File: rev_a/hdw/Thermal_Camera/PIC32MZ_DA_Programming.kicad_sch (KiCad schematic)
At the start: 17 parts

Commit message: added some power supplies
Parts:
- added J?: MRST, symbol Connector_Generic:Conn_02x01
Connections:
- net +3.3V: now also J?.1 (Pin_1)
- net at R?.1, SW?.2: now also J?.2 (Pin_2)
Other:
- moved on the sheet: SW?
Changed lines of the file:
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@@
     (company "Drew Maatman and Michael Laffin")
   )
+  (junction (at 69.85 139.7) (diameter 0) (color 0 0 0 0)
+  )
   (junction (at 106.68 139.7) (diameter 0) (color 0 0 0 0)
+  )
+  (junction (at 86.36 139.7) (diameter 0) (color 0 0 0 0)
   )
   (junction (at 96.52 49.53) (diameter 0) (color 0 0 0 0)
@@
     (stroke (width 0) (type default))
   )
+  (wire (pts (xy 86.36 139.7) (xy 83.82 139.7))
+    (stroke (width 0) (type default))
+  )
   (wire (pts (xy 102.87 71.12) (xy 102.87 54.61))
     (stroke (width 0) (type default))
@@
     (stroke (width 0) (type default))
   )
+  (wire (pts (xy 86.36 139.7) (xy 86.36 147.32))
+    (stroke (width 0) (type default))
+  )
   (wire (pts (xy 90.17 71.12) (xy 90.17 46.99))
     (stroke (width 0) (type default))
@@
     (stroke (width 0) (type default))
   )
+  (wire (pts (xy 72.39 147.32) (xy 69.85 147.32))
+    (stroke (width 0) (type default))
+  )
   (wire (pts (xy 135.255 52.07) (xy 176.53 52.07))
     (stroke (width 0) (type default))
@@
     (stroke (width 0) (type default))
   )
-  (wire (pts (xy 74.93 139.7) (xy 78.74 139.7))
+  (wire (pts (xy 85.09 147.32) (xy 86.36 147.32))
+    (stroke (width 0) (type default))
+  )
+  (wire (pts (xy 69.85 139.7) (xy 73.66 139.7))
     (stroke (width 0) (type default))
   )
@@
     (stroke (width 0) (type default))
   )
+  (wire (pts (xy 69.85 147.32) (xy 69.85 139.7))
+    (stroke (width 0) (type default))
+  )
   (wire (pts (xy 134.62 126.365) (xy 147.955 126.365))
     (stroke (width 0) (type default))
   )
-  (wire (pts (xy 74.93 138.43) (xy 74.93 139.7))
-    (stroke (width 0) (type default))
-  )
-  (wire (pts (xy 91.44 139.7) (xy 88.9 139.7))
+  (wire (pts (xy 69.85 138.43) (xy 69.85 139.7))
+    (stroke (width 0) (type default))
+  )
+  (wire (pts (xy 91.44 139.7) (xy 86.36 139.7))
     (stroke (width 0) (type default))
   )
@@
     )
   )
-  (symbol (lib_id "Switch:SW_Push") (at 83.82 139.7 0) (unit 1)
-    (in_bom yes) (on_board yes) (dnp no)
-    (property "Reference" "SW?" (at 83.82 132.461 0)
-      (effects (font (size 1.27 1.27)))
-    )
-    (property "Value" "MRST" (at 83.82 134.7724 0)
-      (effects (font (size 1.27 1.27)))
-    )
-    (property "Footprint" "Button_Switch_THT:SW_PUSH_6mm" (at 83.82 134.62 0)
-      (effects (font (size 1.27 1.27)) hide)
-    )
-    (property "Datasheet" "" (at 83.82 134.62 0)
+  (symbol (lib_id "Switch:SW_Push") (at 78.74 139.7 0) (unit 1)
+    (in_bom yes) (on_board yes) (dnp no)
+    (property "Reference" "SW?" (at 78.74 132.461 0)
+      (effects (font (size 1.27 1.27)))
+    )
+    (property "Value" "MRST" (at 78.74 134.7724 0)
+      (effects (font (size 1.27 1.27)))
+    )
+    (property "Footprint" "Button_Switch_THT:SW_PUSH_6mm" (at 78.74 134.62 0)
+      (effects (font (size 1.27 1.27)) hide)
+    )
+    (property "Datasheet" "" (at 78.74 134.62 0)
       (effects (font (size 1.27 1.27)) hide)
     )
@@
         (path "/4bd21e0b-5408-4b93-866e-c82ac5b31fa9/c8b41008-ee29-40ae-a4f4-13001b750237"
           (reference "SW?") (unit 1)
+        )
+      )
+    )
+  )
+  (symbol (lib_id "Connector_Generic:Conn_02x01") (at 77.47 147.32 0) (unit 1)
+    (in_bom yes) (on_board yes) (dnp no)
+    (property "Reference" "J?" (at 78.74 144.78 0)
+      (effects (font (size 1.27 1.27)))
+    )
+    (property "Value" "MRST" (at 78.74 149.86 0)
+      (effects (font (size 1.27 1.27)))
+    )
+    (property "Footprint" "" (at 77.47 147.32 0)
+      (effects (font (size 1.27 1.27)) hide)
+    )
+    (property "Datasheet" "~" (at 77.47 147.32 0)
+      (effects (font (size 1.27 1.27)) hide)
+    )
+    (pin "2")
+    (pin "1")
+    (instances
+      (project "Thermal_Camera"
+        (path "/4bd21e0b-5408-4b93-866e-c82ac5b31fa9/c8b41008-ee29-40ae-a4f4-13001b750237"
+          (reference "J?") (unit 1)
         )
       )
@@
     )
   )
-  (symbol (lib_id "power:+3.3V") (at 74.93 138.43 0) (unit 1)
-    (in_bom yes) (on_board yes) (dnp no)
-    (property "Reference" "#PWR?" (at 74.93 142.24 0)
-      (effects (font (size 1.27 1.27)) hide)
-    )
-    (property "Value" "+3.3V" (at 74.93 134.874 0)
-      (effects (font (size 1.27 1.27)))
-    )
-    (property "Footprint" "" (at 74.93 138.43 0)
-      (effects (font (size 1.27 1.27)) hide)
-    )
-    (property "Datasheet" "" (at 74.93 138.43 0)
-      (effects (font (size 1.27 1.27)) hide)
-    )
+  (symbol (lib_id "power:+3.3V") (at 69.85 138.43 0) (unit 1)
+    (in_bom yes) (on_board yes) (dnp no)
+    (property "Reference" "#PWR?" (at 69.85 142.24 0)
+      (effects (font (size 1.27 1.27)) hide)
+    )
+    (property "Value" "+3.3V" (at 69.85 134.874 0)
+      (effects (font (size 1.27 1.27)))
+    )
+    (property "Footprint" "" (at 69.85 138.43 0)
+      (effects (font (size 1.27 1.27)) hide)
+    )
+    (property "Datasheet" "" (at 69.85 138.43 0)
+      (effects (font (size 1.27 1.27)) hide)
+    )

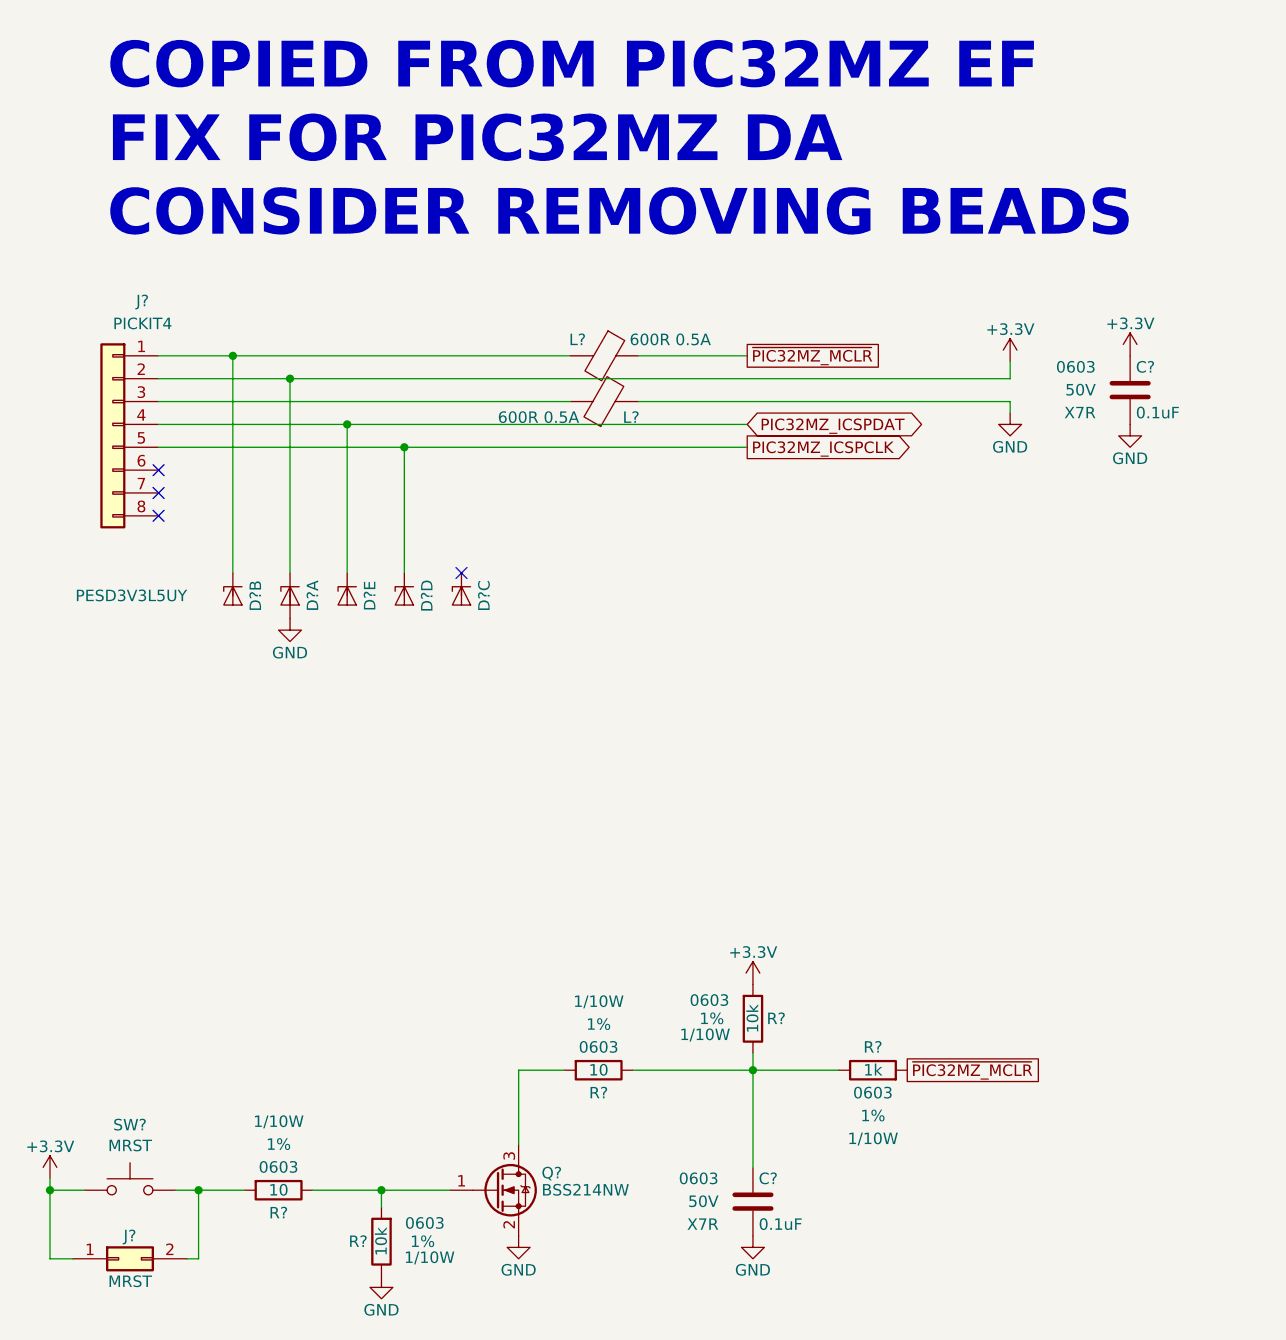
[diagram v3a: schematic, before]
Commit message: changed a lot of circuits from +3.3V to +3.0V VDD
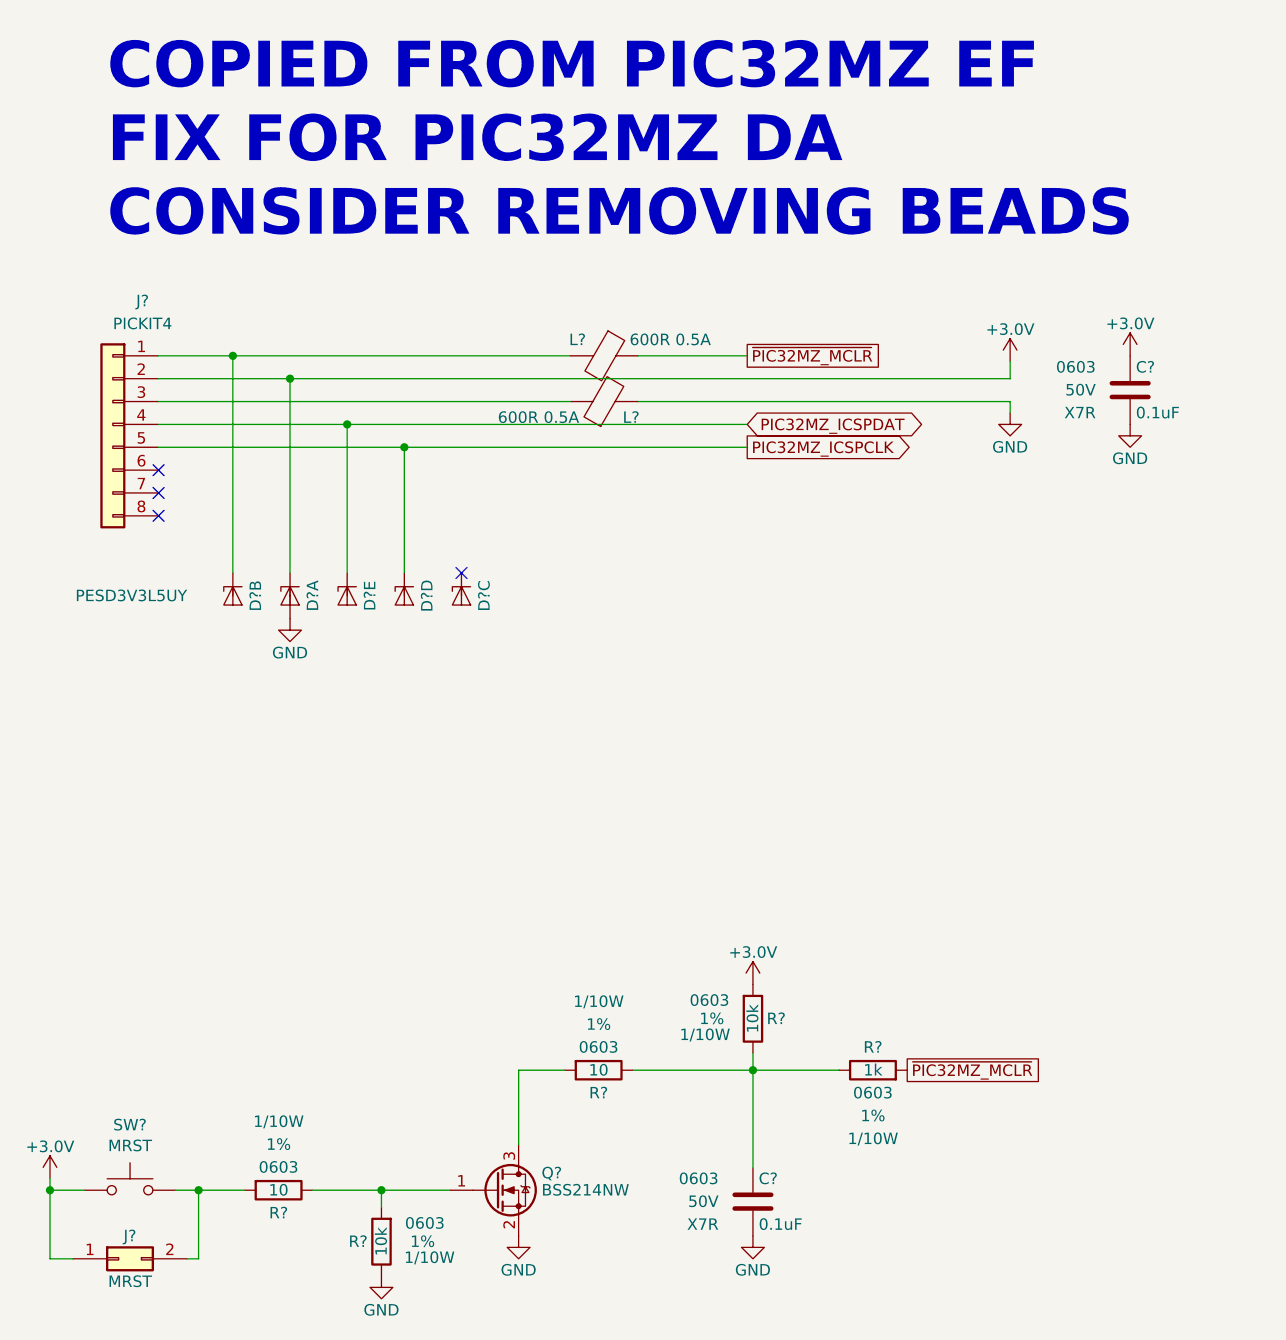
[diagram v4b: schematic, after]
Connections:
- net +3.3V renamed +3.0V
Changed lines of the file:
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@@
+    )
+  )
+  (symbol (lib_id "Custom Library:+3.0V") (at 147.955 116.84 0) (unit 1)
+    (in_bom yes) (on_board yes) (dnp no)
+    (property "Reference" "#PWR01503" (at 147.955 120.65 0)
+      (effects (font (size 1.27 1.27)) hide)
+    )
+    (property "Value" "+3.0V" (at 147.955 113.284 0)
+      (effects (font (size 1.27 1.27)))
+    )
+    (property "Footprint" "" (at 147.955 116.84 0)
+      (effects (font (size 1.27 1.27)) hide)
+    )
+    (property "Datasheet" "" (at 147.955 116.84 0)
+      (effects (font (size 1.27 1.27)) hide)
+    )
+    (pin "1")
+    (instances
+      (project "Thermal_Camera"
+        (path "/4bd21e0b-5408-4b93-866e-c82ac5b31fa9/c8b41008-ee29-40ae-a4f4-13001b750237"
+          (reference "#PWR01503") (unit 1)
+        )
+      )
     )
   )
@@
     )
   )
+  (symbol (lib_id "Custom Library:+3.0V") (at 69.85 138.43 0) (unit 1)
+    (in_bom yes) (on_board yes) (dnp no)
+    (property "Reference" "#PWR01504" (at 69.85 142.24 0)
+      (effects (font (size 1.27 1.27)) hide)
+    )
+    (property "Value" "+3.0V" (at 69.85 134.874 0)
+      (effects (font (size 1.27 1.27)))
+    )
+    (property "Footprint" "" (at 69.85 138.43 0)
+      (effects (font (size 1.27 1.27)) hide)
+    )
+    (property "Datasheet" "" (at 69.85 138.43 0)
+      (effects (font (size 1.27 1.27)) hide)
+    )
+    (pin "1")
+    (instances
+      (project "Thermal_Camera"
+        (path "/4bd21e0b-5408-4b93-866e-c82ac5b31fa9/c8b41008-ee29-40ae-a4f4-13001b750237"
+          (reference "#PWR01504") (unit 1)
+        )
+      )
+    )
+  )
   (symbol (lib_id "Power_Protection:PESD3V3L5UY") (at 90.17 73.66 270) (unit 2)
     (in_bom yes) (on_board yes) (dnp no)
@@
     )
   )
-  (symbol (lib_id "power:+3.3V") (at 147.955 116.84 0) (unit 1)
-    (in_bom yes) (on_board yes) (dnp no)
-    (property "Reference" "#PWR?" (at 147.955 120.65 0)
-      (effects (font (size 1.27 1.27)) hide)
-    )
-    (property "Value" "+3.3V" (at 147.955 113.284 0)
-      (effects (font (size 1.27 1.27)))
-    )
-    (property "Footprint" "" (at 147.955 116.84 0)
-      (effects (font (size 1.27 1.27)) hide)
-    )
-    (property "Datasheet" "" (at 147.955 116.84 0)
-      (effects (font (size 1.27 1.27)) hide)
-    )
-    (pin "1")
-    (instances
-      (project "Analog_Clock"
-        (path "/0dc9b974-a945-4291-bc55-04b8e342b0e5/00000000-0000-0000-0000-00005e939eaf"
-          (reference "#PWR?") (unit 1)
-        )
-      )
-      (project "Nixie_Clock_Core"
-        (path "/16fdce21-b570-4d81-a458-e8839d611806/0953f70f-0c64-48c1-b5cf-d1f41f95ef1f"
-          (reference "#PWR0805") (unit 1)
-        )
-      )
-      (project "Thermal_Camera"
-        (path "/4bd21e0b-5408-4b93-866e-c82ac5b31fa9/c8b41008-ee29-40ae-a4f4-13001b750237"
-          (reference "#PWR0905") (unit 1)
-        )
-      )
-    )
-  )
   (symbol (lib_id "Custom_Library:C_Custom") (at 189.865 50.8 0) (unit 1)
     (in_bom yes) (on_board yes) (dnp no)
@@
         (path "/4bd21e0b-5408-4b93-866e-c82ac5b31fa9/c8b41008-ee29-40ae-a4f4-13001b750237"
           (reference "C?") (unit 1)
+        )
+      )
+    )
+  )
+  (symbol (lib_id "Custom Library:+3.0V") (at 176.53 47.625 0) (unit 1)
+    (in_bom yes) (on_board yes) (dnp no)
+    (property "Reference" "#PWR01502" (at 176.53 51.435 0)
+      (effects (font (size 1.27 1.27)) hide)
+    )
+    (property "Value" "+3.0V" (at 176.53 44.069 0)
+      (effects (font (size 1.27 1.27)))
+    )
+    (property "Footprint" "" (at 176.53 47.625 0)
+      (effects (font (size 1.27 1.27)) hide)
+    )
+    (property "Datasheet" "" (at 176.53 47.625 0)
+      (effects (font (size 1.27 1.27)) hide)
+    )
+    (pin "1")
+    (instances
+      (project "Thermal_Camera"
+        (path "/4bd21e0b-5408-4b93-866e-c82ac5b31fa9/c8b41008-ee29-40ae-a4f4-13001b750237"
+          (reference "#PWR01502") (unit 1)
         )
       )
@@
     )
   )
-  (symbol (lib_id "power:+3.3V") (at 176.53 47.625 0) (unit 1)
-    (in_bom yes) (on_board yes) (dnp no)
-    (property "Reference" "#PWR?" (at 176.53 51.435 0)
-      (effects (font (size 1.27 1.27)) hide)
-    )
-    (property "Value" "+3.3V" (at 176.53 44.069 0)
-      (effects (font (size 1.27 1.27)))
-    )
-    (property "Footprint" "" (at 176.53 47.625 0)
-      (effects (font (size 1.27 1.27)) hide)
-    )
-    (property "Datasheet" "" (at 176.53 47.625 0)
-      (effects (font (size 1.27 1.27)) hide)
-    )
-    (pin "1")
-    (instances
-      (project "Analog_Clock"
-        (path "/0dc9b974-a945-4291-bc55-04b8e342b0e5/00000000-0000-0000-0000-00005e939eaf"
-          (reference "#PWR?") (unit 1)
-        )
-      )
-      (project "Nixie_Clock_Core"
-        (path "/16fdce21-b570-4d81-a458-e8839d611806/0953f70f-0c64-48c1-b5cf-d1f41f95ef1f"
-          (reference "#PWR0807") (unit 1)
-        )
-      )
-      (project "Thermal_Camera"
-        (path "/4bd21e0b-5408-4b93-866e-c82ac5b31fa9/c8b41008-ee29-40ae-a4f4-13001b750237"
-          (reference "#PWR0907") (unit 1)
-        )
-      )
-    )
-  )
   (symbol (lib_id "Power_Protection:PESD3V3L5UY") (at 109.22 73.66 270) (unit 4)
     (in_bom yes) (on_board yes) (dnp no)
@@
     )
   )
+  (symbol (lib_id "Custom Library:+3.0V") (at 189.865 46.99 0) (unit 1)
+    (in_bom yes) (on_board yes) (dnp no)
+    (property "Reference" "#PWR01501" (at 189.865 50.8 0)
+      (effects (font (size 1.27 1.27)) hide)
+    )
+    (property "Value" "+3.0V" (at 189.865 43.434 0)
+      (effects (font (size 1.27 1.27)))
+    )
+    (property "Footprint" "" (at 189.865 46.99 0)
+      (effects (font (size 1.27 1.27)) hide)
+    )
+    (property "Datasheet" "" (at 189.865 46.99 0)
+      (effects (font (size 1.27 1.27)) hide)
+    )
+    (pin "1")
+    (instances
+      (project "Thermal_Camera"
+        (path "/4bd21e0b-5408-4b93-866e-c82ac5b31fa9/c8b41008-ee29-40ae-a4f4-13001b750237"
+          (reference "#PWR01501") (unit 1)
+        )
+      )
+    )
+  )
   (symbol (lib_id "Custom_Library:C_Custom") (at 147.955 140.97 0) (unit 1)
     (in_bom yes) (on_board yes) (dnp no)
@@
     )
   )
-  (symbol (lib_id "power:+3.3V") (at 69.85 138.43 0) (unit 1)
-    (in_bom yes) (on_board yes) (dnp no)
-    (property "Reference" "#PWR?" (at 69.85 142.24 0)
-      (effects (font (size 1.27 1.27)) hide)
-    )
-    (property "Value" "+3.3V" (at 69.85 134.874 0)
-      (effects (font (size 1.27 1.27)))
-    )
-    (property "Footprint" "" (at 69.85 138.43 0)
-      (effects (font (size 1.27 1.27)) hide)
-    )
-    (property "Datasheet" "" (at 69.85 138.43 0)
-      (effects (font (size 1.27 1.27)) hide)
-    )
-    (pin "1")
-    (instances
-      (project "Analog_Clock"
-        (path "/0dc9b974-a945-4291-bc55-04b8e342b0e5/00000000-0000-0000-0000-00005e939eaf"
-          (reference "#PWR?") (unit 1)
-        )
-      )
-      (project "Nixie_Clock_Core"
-        (path "/16fdce21-b570-4d81-a458-e8839d611806/0953f70f-0c64-48c1-b5cf-d1f41f95ef1f"
-          (reference "#PWR0801") (unit 1)
-        )
-      )
-      (project "Thermal_Camera"
-        (path "/4bd21e0b-5408-4b93-866e-c82ac5b31fa9/c8b41008-ee29-40ae-a4f4-13001b750237"
-          (reference "#PWR0901") (unit 1)
-        )
-      )
-    )
-  )
   (symbol (lib_id "Device:Ferrite_Bead") (at 131.445 46.99 270) (unit 1)
     (in_bom yes) (on_board yes) (dnp no)
@@
         )
       )
-    )
-  )
-  (symbol (lib_id "power:+3.3V") (at 189.865 46.99 0) (unit 1)
-    (in_bom yes) (on_board yes) (dnp no)
-    (property "Reference" "#PWR?" (at 189.865 50.8 0)
-      (effects (font (size 1.27 1.27)) hide)
-    )
-    (property "Value" "+3.3V" (at 189.865 43.434 0)
-      (effects (font (size 1.27 1.27)))
-    )
-    (property "Footprint" "" (at 189.865 46.99 0)
-      (effects (font (size 1.27 1.27)) hide)
-    )
-    (property "Datasheet" "" (at 189.865 46.99 0)
-      (effects (font (size 1.27 1.27)) hide)
-    )
-    (pin "1")
-    (instances
-      (project "Analog_Clock"
-        (path "/0dc9b974-a945-4291-bc55-04b8e342b0e5/00000000-0000-0000-0000-00005e939eaf"
-          (reference "#PWR?") (unit 1)
-        )
-      )
-      (project "Nixie_Clock_Core"
-        (path "/16fdce21-b570-4d81-a458-e8839d611806/0953f70f-0c64-48c1-b5cf-d1f41f95ef1f"
-          (reference "#PWR0809") (unit 1)
-        )
-      )
-      (project "Thermal_Camera"
-        (path "/4bd21e0b-5408-4b93-866e-c82ac5b31fa9/c8b41008-ee29-40ae-a4f4-13001b750237"
-          (reference "#PWR0909") (unit 1)
-        )
-      )

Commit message: added PIC32 bypass, SD card load switch, other random junk
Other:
- note removed: "COPIED FROM PIC32MZ EF FIX FOR PIC32MZ DA CONSIDER REMOVING BEADS"
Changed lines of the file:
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@@
     (stroke (width 0) (type default))
-  )
-  (text "COPIED FROM PIC32MZ EF\nFIX FOR PIC32MZ DA\nCONSIDER REMOVING BEADS"
-    (at 76.2 34.29 0)
-    (effects (font (size 5.08 5.08) (thickness 1.016) bold (color 194 0 0 1)) (justify left bottom))
   )
   (global_label "~{PIC32MZ_MCLR}" (shape passive) (at 147.32 46.99 0) (fields_autoplaced)
